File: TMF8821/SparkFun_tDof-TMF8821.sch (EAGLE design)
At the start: 28 parts, among them J4 QWIIC_RIGHT_ANGLE, J5 QWIIC_RIGHT_ANGLE

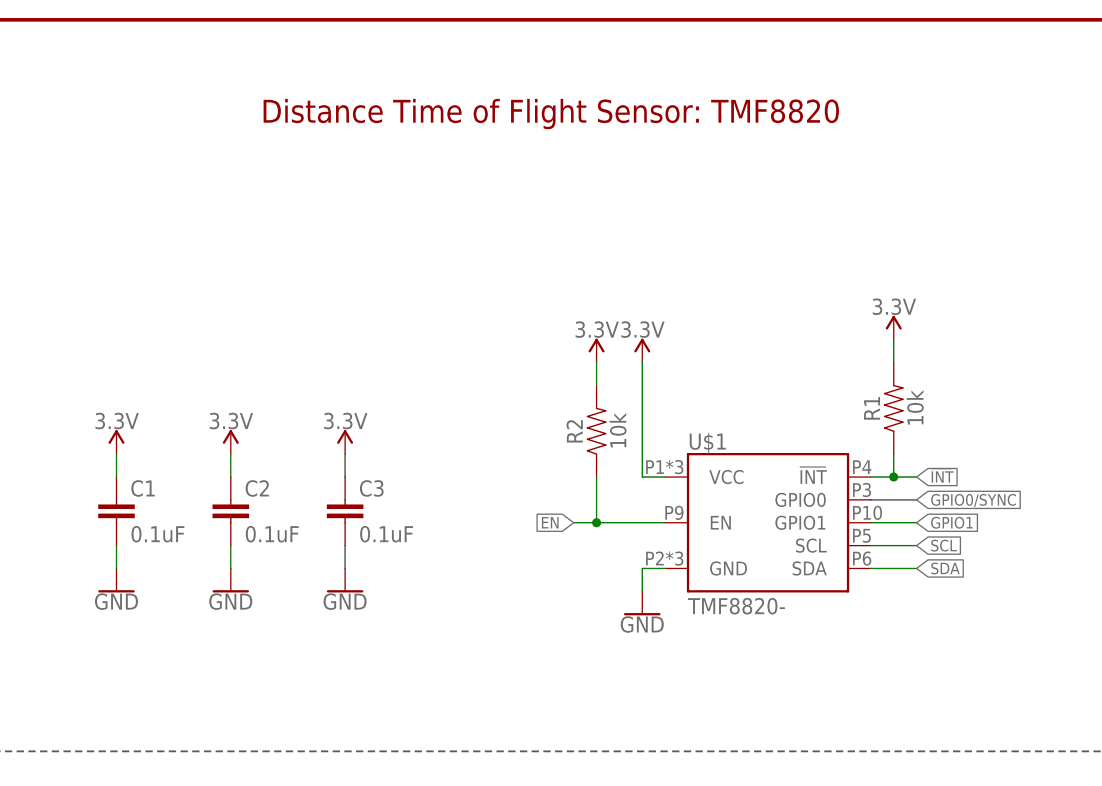
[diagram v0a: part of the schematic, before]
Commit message: Adds "TMF8821" silk to the 8821 board design files
* Replaces device with TMF8821 in schematic and updates text
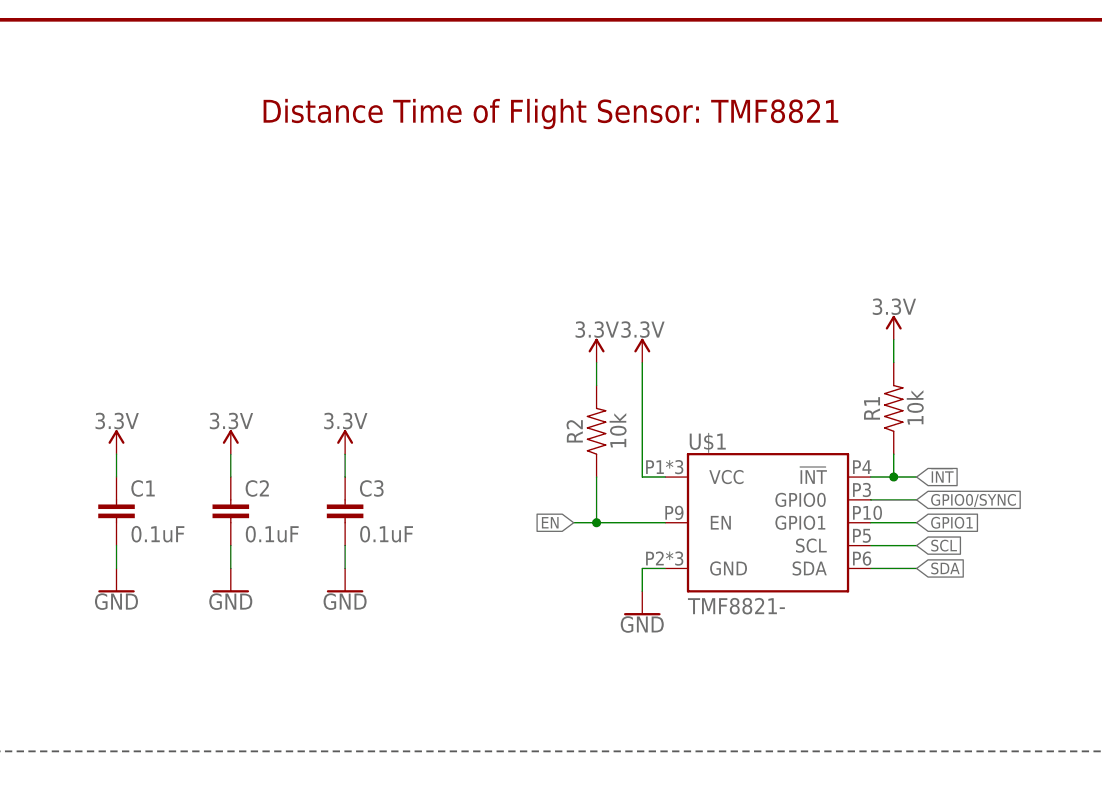
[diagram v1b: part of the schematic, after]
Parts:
- U$1: value TMF8820- -> TMF8821-; device TMF882X:TMF8820- -> TMF882X:TMF8821-
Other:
- note added: "Distance Time of Flight Sensor: TMF8821"
- note removed: "Distance Time of Flight Sensor: TMF8820"
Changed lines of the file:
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@@
 <part name="I2C" library="SparkFun-Jumpers" deviceset="JUMPER-SMT_3_2-NC_TRACE" device="_SILK" package3d_urn="urn:adsk.eagle:package:39289/1" value="I2C_PU"/>
 <part name="SUPPLY10" library="SparkFun-PowerSymbols" deviceset="3.3V" device=""/>
-<part name="U$1" library="TMF882X" deviceset="TMF8820" device="-"/>
+<part name="U$1" library="TMF882X" deviceset="TMF8821" device="-"/>
 <part name="C1" library="SparkFun-Capacitors" deviceset="0.1UF" device="-0402T-6.3V-10%-X7R" value="0.1uF"/>
 <part name="C2" library="SparkFun-Capacitors" deviceset="0.1UF" device="-0402T-6.3V-10%-X7R" value="0.1uF"/>
@@
 pull up resistors.</text>
 <text x="168.148" y="11.176" size="2.54" layer="94" font="vector">Elias Santistevan</text>
-<text x="73.66" y="175.26" size="2.54" layer="94" font="vector" align="center">Distance Time of Flight Sensor: TMF8820</text>
+<text x="73.66" y="175.26" size="2.54" layer="94" font="vector" align="center">Distance Time of Flight Sensor: TMF8821</text>
 <wire x1="0" y1="104.14" x2="144.78" y2="104.14" width="0.2032" layer="97" style="longdash"/>
 <wire x1="144.78" y1="104.14" x2="248.92" y2="104.14" width="0.2032" layer="97" style="longdash"/>

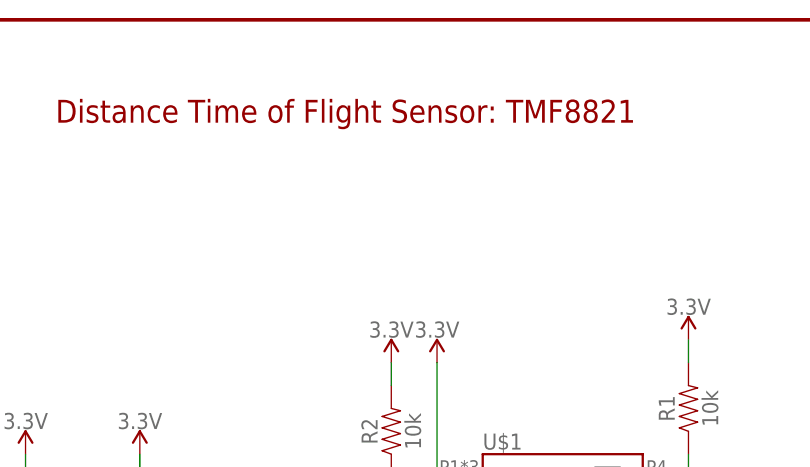
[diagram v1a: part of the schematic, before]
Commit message: Adds VCC Range to schematic in both designs
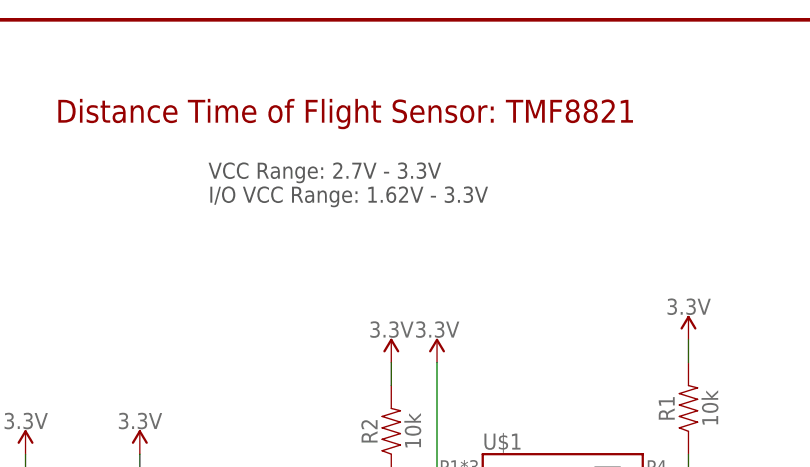
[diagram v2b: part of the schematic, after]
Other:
- note added: "VCC Range: 2.7V - 3.3V I/O VCC Range: 1.62V - 3.3V"
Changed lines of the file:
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@@
 <wire x1="144.78" y1="104.14" x2="248.92" y2="104.14" width="0.2032" layer="97" style="longdash"/>
 <wire x1="144.78" y1="185.42" x2="144.78" y2="104.14" width="0.2032" layer="97" style="longdash"/>
+<text x="58.42" y="165.1" size="1.778" layer="97" font="vector">VCC Range: 2.7V - 3.3V
+I/O VCC Range: 1.62V - 3.3V</text>
 </plain>
 <instances>

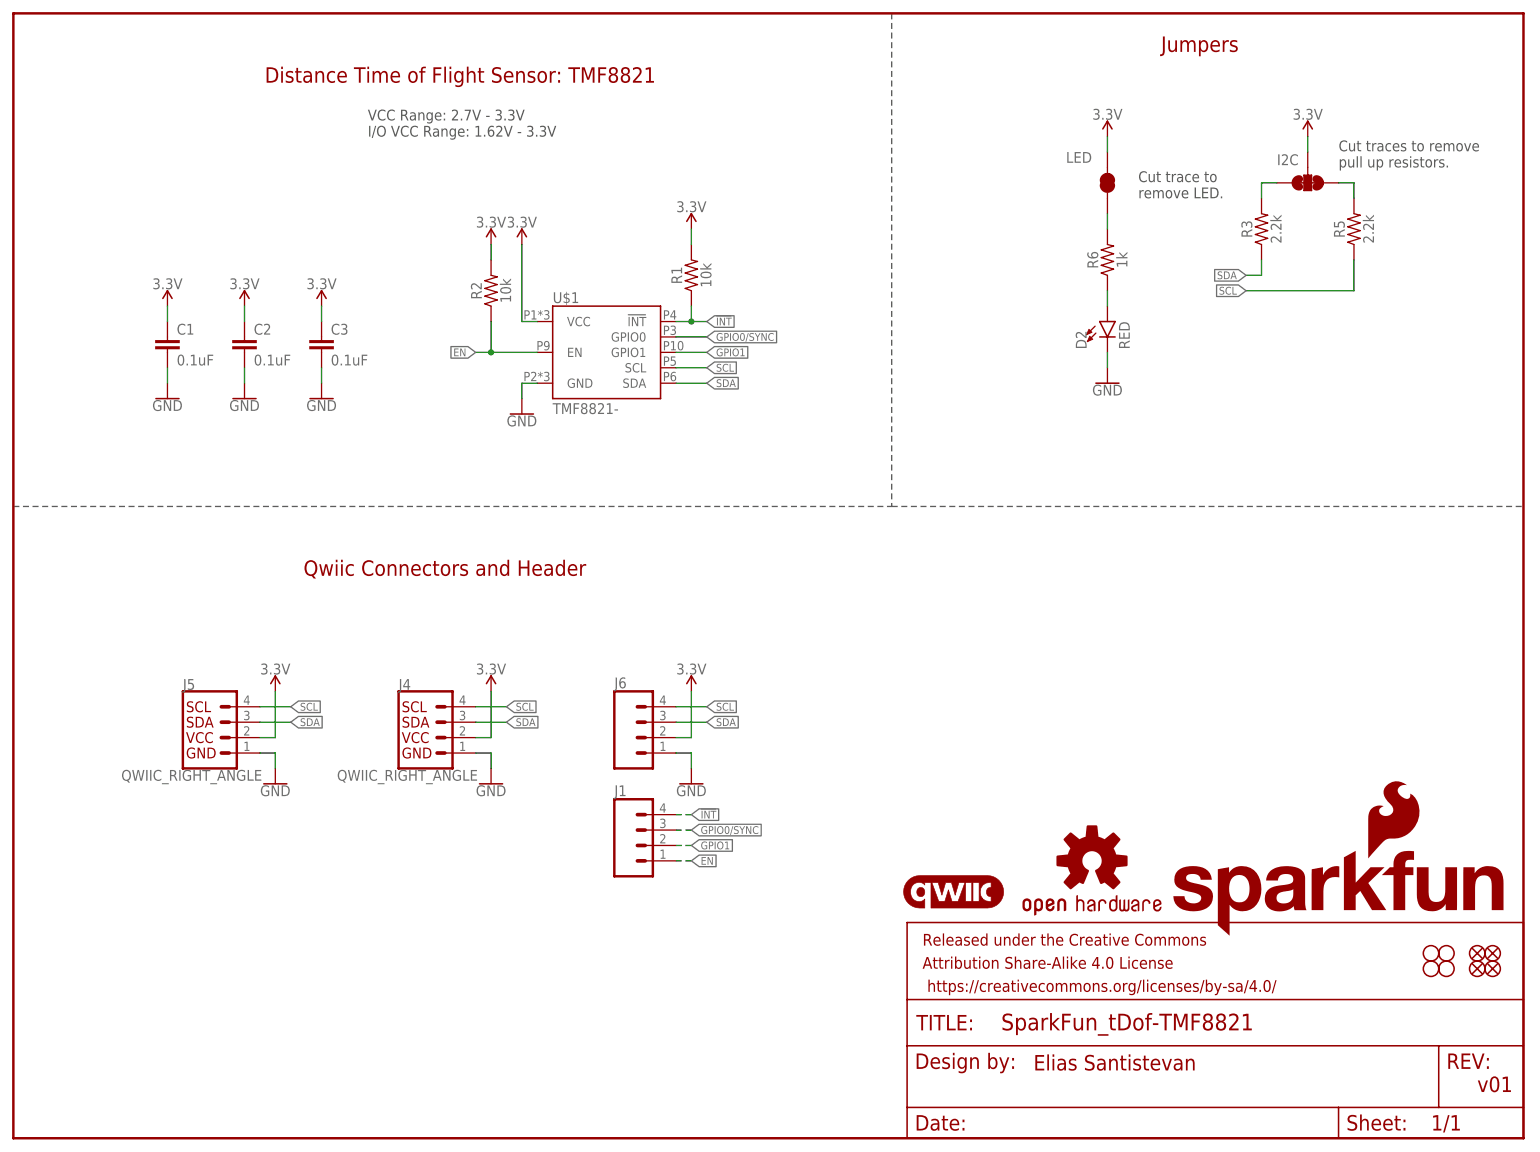
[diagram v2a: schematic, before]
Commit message: Copies 8820 designs to create 8821 designs - updates relevant references to 8820 to 8821
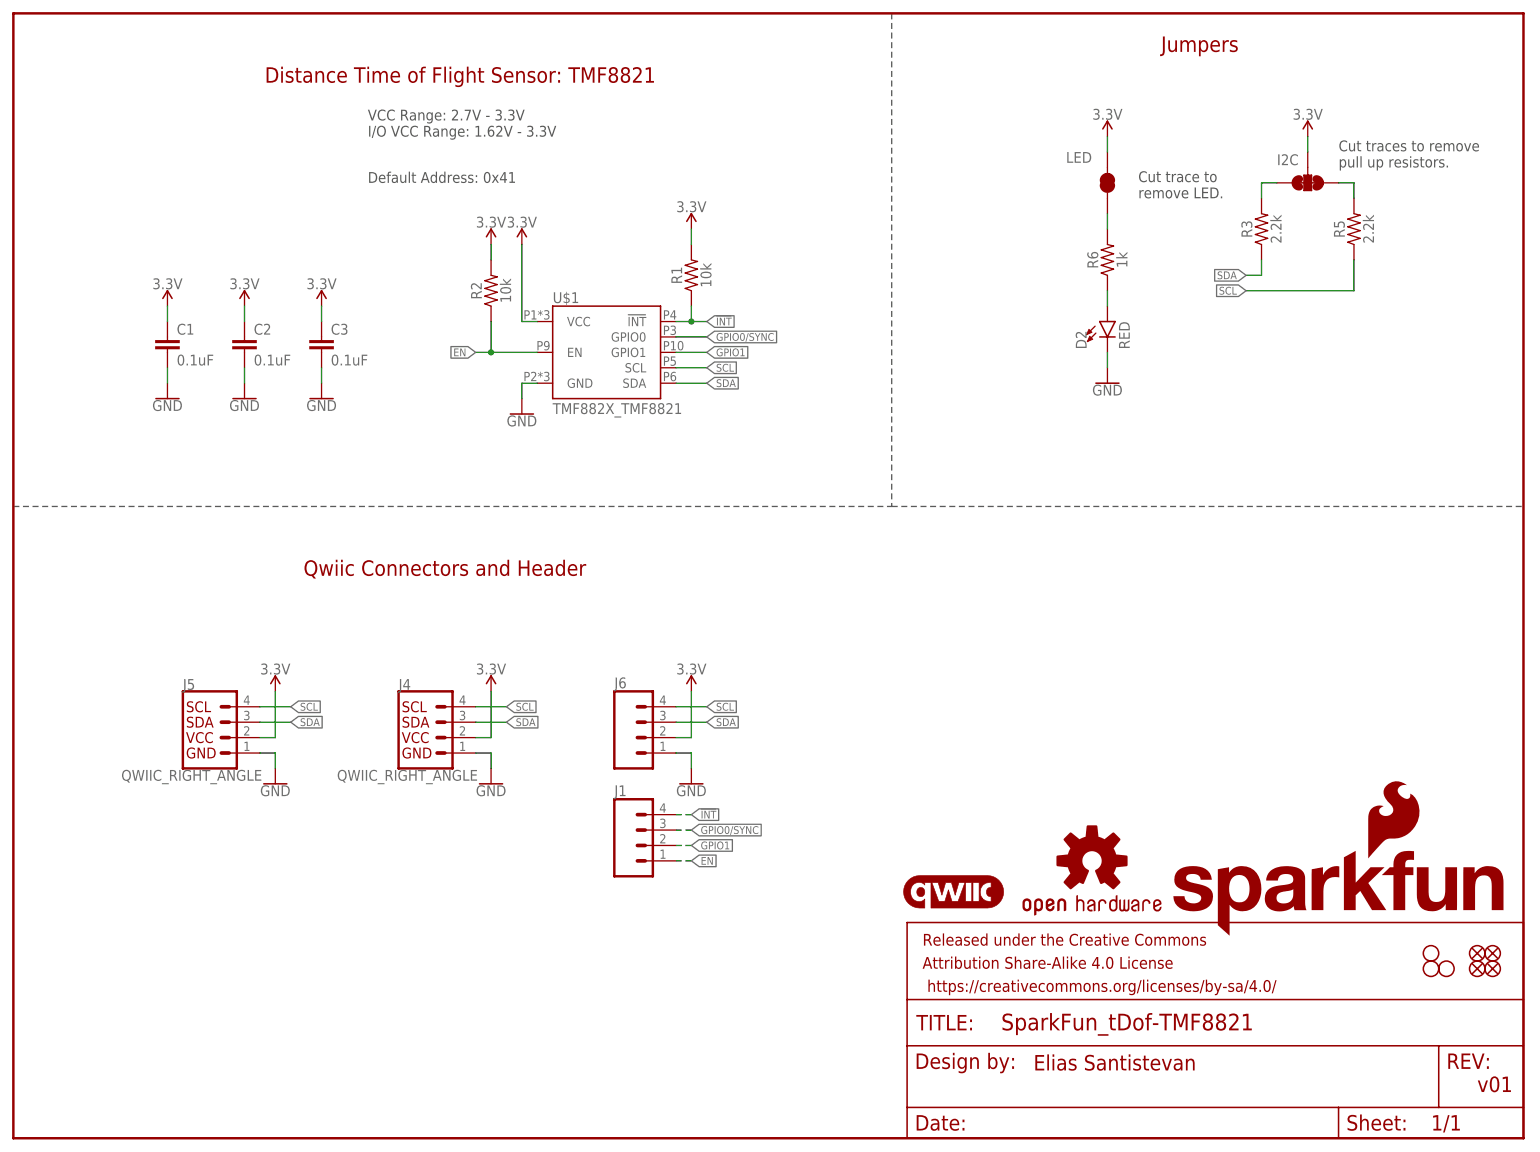
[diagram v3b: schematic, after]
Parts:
- removed H7: STAND-OFFTIGHT, SparkFun-Hardware:STAND-OFFTIGHT
- U$1: value TMF8821- -> TMF882X_TMF8821; device TMF882X:TMF8821- -> TMF882X:TMF882X_TMF8821
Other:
- note added: "Default Address: 0x41"
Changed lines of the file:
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@@
 <part name="H5" library="SparkFun-Hardware" deviceset="STAND-OFF" device="TIGHT"/>
 <part name="H6" library="SparkFun-Hardware" deviceset="STAND-OFF" device="TIGHT"/>
-<part name="H7" library="SparkFun-Hardware" deviceset="STAND-OFF" device="TIGHT"/>
 <part name="H8" library="SparkFun-Hardware" deviceset="STAND-OFF" device="TIGHT"/>
 <part name="J4" library="SparkFun-Connectors" deviceset="QWIIC_CONNECTOR" device="JS-1MM" value="QWIIC_RIGHT_ANGLE"/>
@@
 <part name="I2C" library="SparkFun-Jumpers" deviceset="JUMPER-SMT_3_2-NC_TRACE" device="_SILK" package3d_urn="urn:adsk.eagle:package:39289/1" value="I2C_PU"/>
 <part name="SUPPLY10" library="SparkFun-PowerSymbols" deviceset="3.3V" device=""/>
-<part name="U$1" library="TMF882X" deviceset="TMF8821" device="-"/>
+<part name="U$1" library="TMF882X" deviceset="TMF882X" device="_TMF8821" value="TMF882X_TMF8821"/>
 <part name="C1" library="SparkFun-Capacitors" deviceset="0.1UF" device="-0402T-6.3V-10%-X7R" value="0.1uF"/>
 <part name="C2" library="SparkFun-Capacitors" deviceset="0.1UF" device="-0402T-6.3V-10%-X7R" value="0.1uF"/>
@@
 <text x="58.42" y="165.1" size="1.778" layer="97" font="vector">VCC Range: 2.7V - 3.3V
 I/O VCC Range: 1.62V - 3.3V</text>
+<text x="58.42" y="157.48" size="1.778" layer="97" font="vector">Default Address: 0x41</text>
 </plain>
 <instances>
@@
 <instance part="H5" gate="G$1" x="233.68" y="27.94" smashed="yes"/>
 <instance part="H6" gate="G$1" x="233.68" y="30.48" smashed="yes"/>
-<instance part="H7" gate="G$1" x="236.22" y="30.48" smashed="yes"/>
 <instance part="H8" gate="G$1" x="236.22" y="27.94" smashed="yes"/>
 <instance part="J4" gate="G$1" x="68.58" y="66.04" smashed="yes">
